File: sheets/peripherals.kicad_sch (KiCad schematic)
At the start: 49 parts, among them J3 SM05B-GHS-TB, J4 Header, J5 BM02B-ACHSS-GAN-ETF, J6 SM04B-GHS-TB, J7 SM04B-GHS-TB, J8 SM06B-GHS-TB, J9 SM06B-GHS-TB, Q2 RUM001L02T2CL, U10 SGP41-D-R4, U11 PCA9306D, U12 SRV05-4, U13 BME690

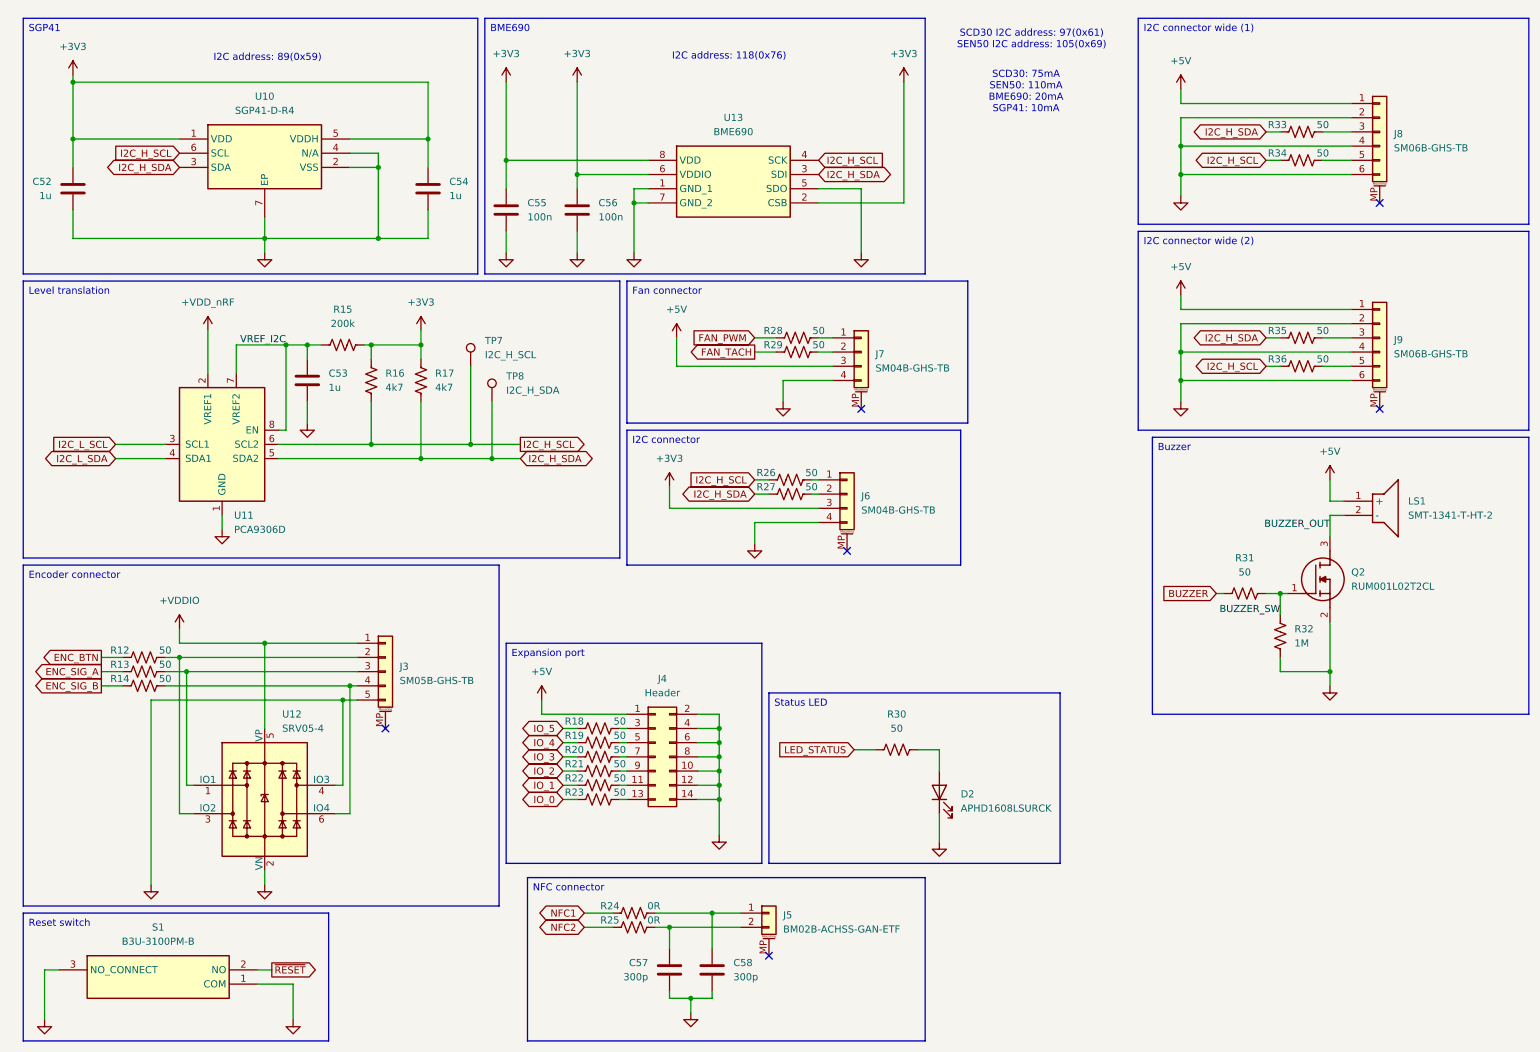
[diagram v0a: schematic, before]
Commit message: Move sheets to a separate folder
The board sheet files have been moved to a sheet folder to make
the repository more readable.
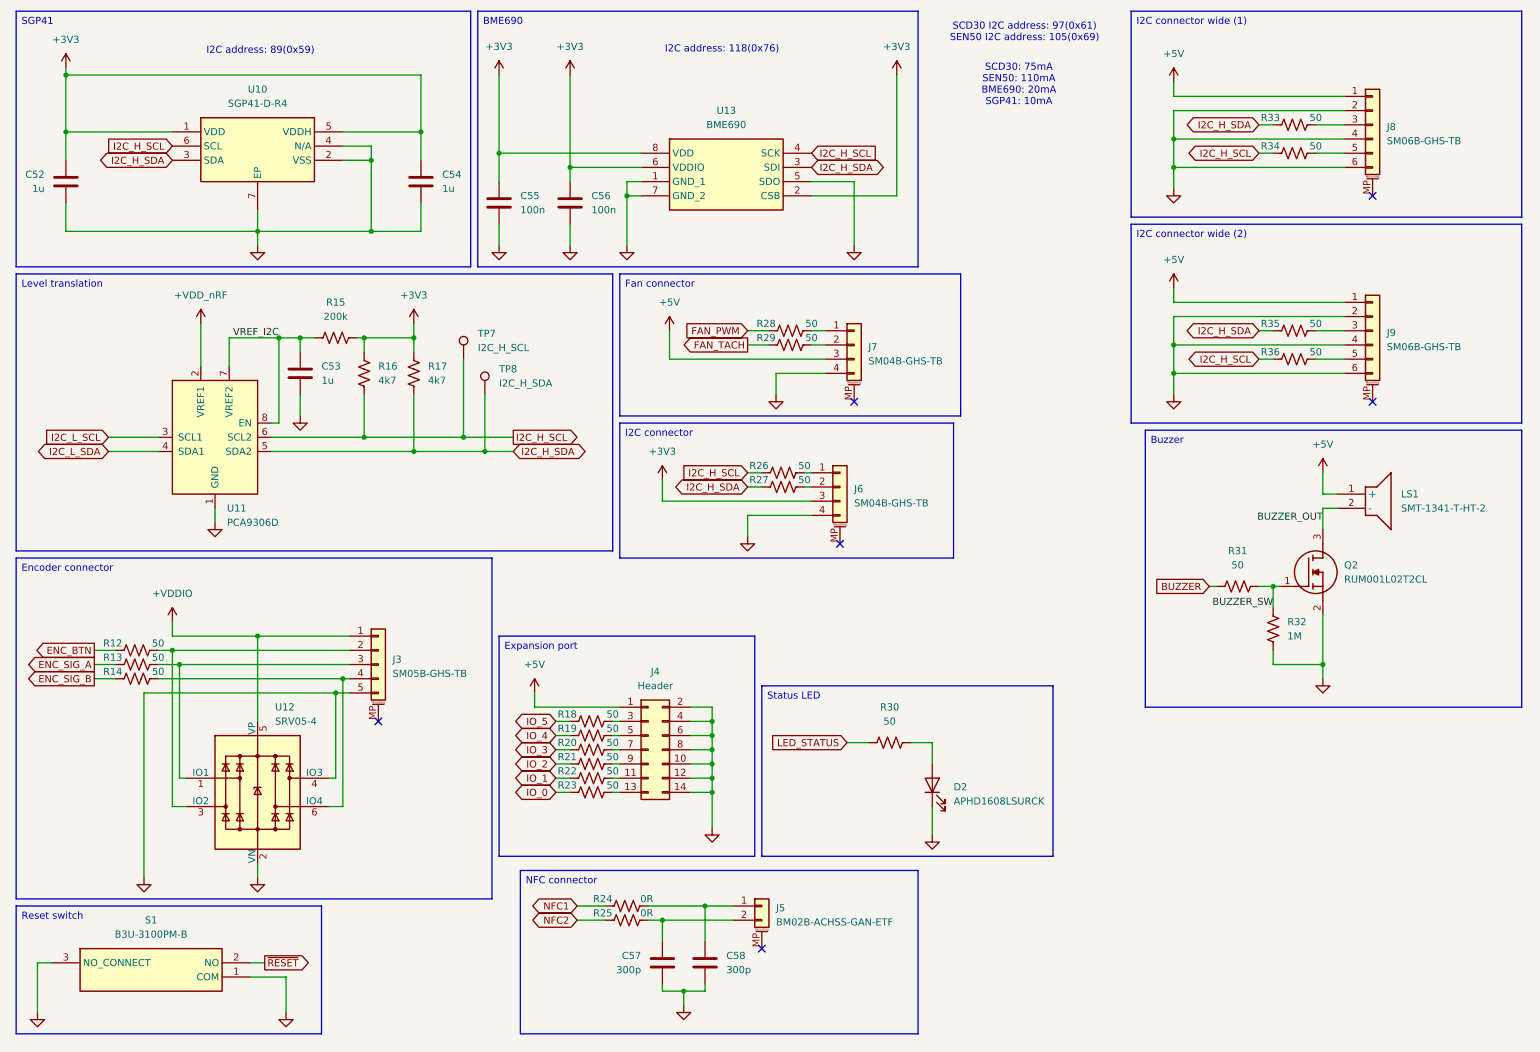
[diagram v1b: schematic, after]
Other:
- moved on the sheet: C52, C53, C54, C55, C56, C57, C58, D2, J3, J4, J5, J6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

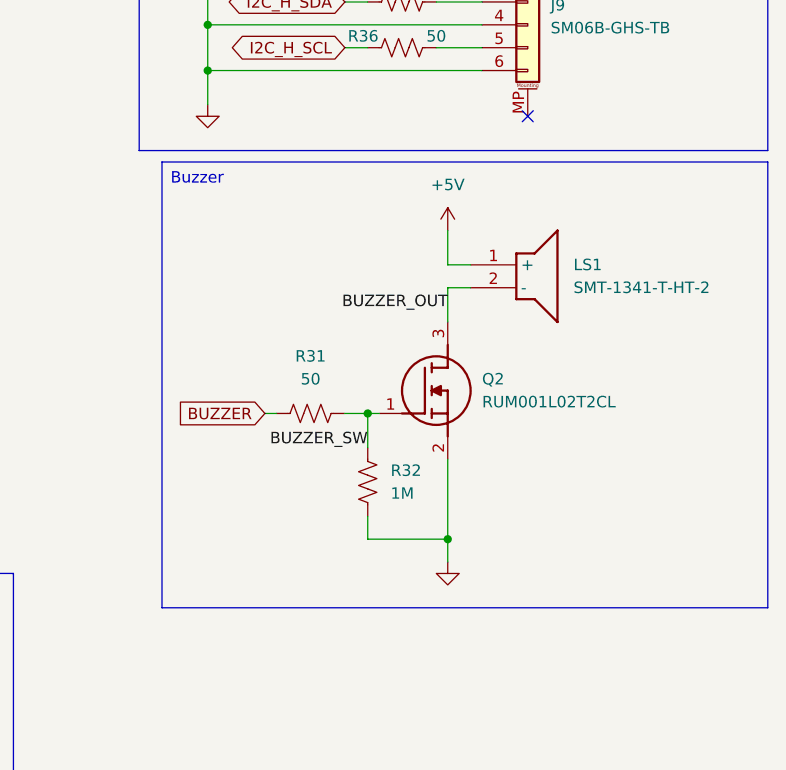
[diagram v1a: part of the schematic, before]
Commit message: Add project symbols and footprints
Move all self-made symbols and footprints to the lib folder.
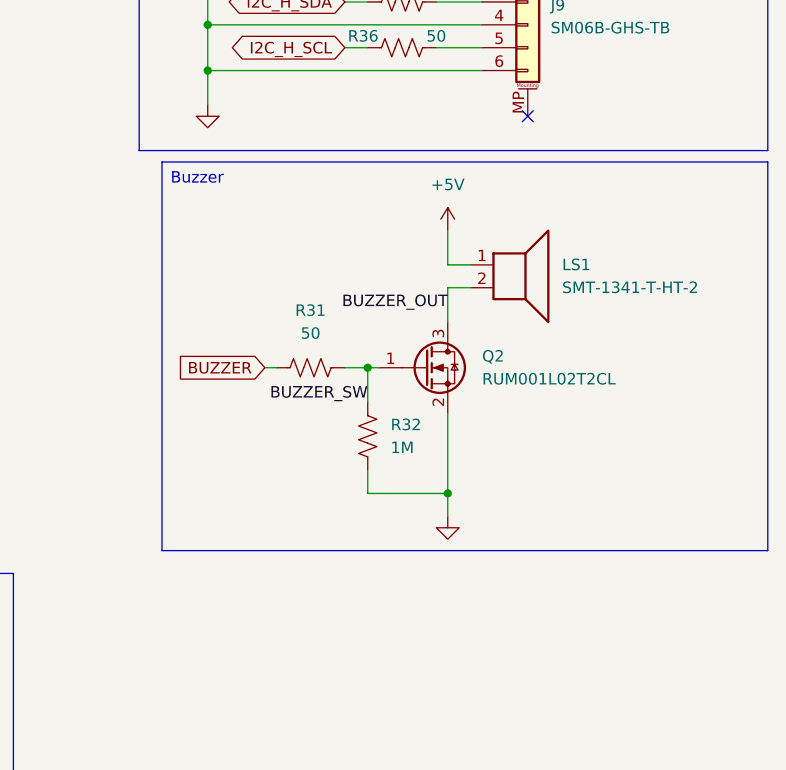
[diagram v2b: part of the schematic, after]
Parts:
- J5: footprint Connector_JST:JST_ACH_BM02B-ACHSS-GAN-ETF_1x02-1MP_P1.20mm_Vertical -> BM02B-ACHSS-GAN-ETF:JST_ACH_BM02B-ACHSS-GAN-ETF_1x02-1MP_P1.20mm_Vertical
- LS1: symbol SMT-1341-T-HT-2:SMT-1341-T-HT-2 -> Device:Speaker
- Q2: symbol RUM001L02T2CL:RUM001L02T2CL -> Transistor_FET:Q_NMOS_GSD
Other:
- moved on the sheet: R31, R32
